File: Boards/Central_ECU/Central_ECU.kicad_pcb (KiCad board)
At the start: 4 copper layers, 100 x 100 mm, 178 parts, among them J1 Micro_SD_Card, J10 Solenoid NANOFIT, J11 DB9 Microfit, J12 RS422 JST, J13 USB_B_Micro, J14 SWD JST PH, J15 UART JST, J2 Extras JST, J3 MICROFIT, J4 Siren MICROFIT, J5 I2CB JST, J6 MICROFIT, J7 I2CA JST, J8 Ignitor JST EH, J9 DB9 MICROFIT, Q1 DMT12H060LFDF, Q2 DMT12H060LFDF, Q3 DMT12H060LFDF, Q4 DMP6023LFG, Q5 DMP6023LFG, SW2 On Switch, U1 SSD1306, U2 STM32G0B1RCTx, U3 TCAN1046, U4 LM339B, U5 LM1084-ADJ, U6 TPS16630PWPR, U7 AZ1117C-5.0, U8 AZ1117C-3.3, U9 LPS22HH, Y1 8MHz, Y2 32.768k

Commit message: More progress on layout
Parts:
- added R49: 10K, Resistor_SMD:R_0603_1608Metric, F.Cu at (147.3, 117.1)
- added R50: 10K, Resistor_SMD:R_0603_1608Metric, F.Cu at (146.6, 118.6)
- C1, C10, C2, C3, C4, C7: moved to B.Cu
- C26, C27: footprint Capacitor_SMD:C_0603_1608Metric -> Capacitor_SMD:C_1206_3216Metric
- C30, C31, C33, C34: footprint Capacitor_SMD:C_0603_1608Metric -> Capacitor_SMD:C_1206_3216Metric; moved to B.Cu
- C6, C8, C9: footprint Capacitor_SMD:C_0603_1608Metric -> Capacitor_SMD:C_0402_1005Metric
- R20, R21, R22: footprint Resistor_SMD:R_0603_1608Metric -> Resistor_SMD:R_1206_3216Metric
- TP12: value ARMSIG -> CONT2
- TP13: value EMCH1 -> CONT1
- TP15: value EMCH2 -> OXSNE
- TP17: value OXFIRE -> SNE12
- TP18: value SENSE12 -> OXFIRE
- TP19: value SENSEOX -> EMCH2
- TP20: value CONT1 -> EMCH1
- TP21: value CONT2 -> ARMSIG
- Y1: footprint Crystal:Crystal_SMD_Abracon_ABM3B-4Pin_5.0x3.2mm -> Crystal:Crystal_SMD_Abracon_ABM8G-4Pin_3.2x2.5mm
- moved R20 241.6 mm to (165.1, 55.9), turned to 90 degrees
- moved J8 237.0 mm to (165.6, 145.8)
- moved J10 227.4 mm to (187.2, 146.0), turned to -90 degrees
- moved U5 226.0 mm to (179.7, 56.4)
- moved Q3 220.5 mm to (168.1, 142.2), turned to 180 degrees
- moved R36 219.1 mm to (164.8, 142.7), turned to 180 degrees
- moved C35 219.0 mm to (164.8, 139.7)
- moved R38 218.6 mm to (164.8, 141.2)
- moved C34 217.9 mm to (167.1, 148.1)
- moved C33 217.6 mm to (167.1, 143.5)
- moved C18 217.2 mm to (187.6, 106.4), turned to 180 degrees
- moved D15 217.0 mm to (170.7, 142.7), turned to 180 degrees
- moved R37 214.3 mm to (169.2, 138.9), turned to -90 degrees
- moved R39 214.1 mm to (169.2, 135.9), turned to -90 degrees
- moved J11 213.9 mm to (192.5, 121.8), turned to 90 degrees
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- renumbered ARM to SW1
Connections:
- C29 pad 1: /EMATCH_2_CONT -> /ARM_HS
- R25 pad 1: /12V_SENSE -> /OX_FIRE
- R26 pad 2: /12V_SENSE -> /OX_FIRE
- R30 pad 1: /EMATCH_2_CONT -> /ARM_HS
- R33 pad 1: /OX_LOW_SENSE -> /EMATCH_2_FIRE
- R35 pad 2: /OX_LOW_SENSE -> /EMATCH_2_FIRE
- R37 pad 1: /EMATCH_1_CONT -> /EMATCH_1_FIRE
- R39 pad 2: /EMATCH_1_CONT -> /EMATCH_1_FIRE
- TP12 pad 1: /ARM_HS -> /EMATCH_2_CONT
- TP13 pad 1: /EMATCH_1_FIRE -> /EMATCH_1_CONT
- TP15 pad 1: /EMATCH_2_FIRE -> /OX_LOW_SENSE
- TP17 pad 1: /OX_FIRE -> /12V_SENSE
- TP18 pad 1: /12V_SENSE -> /OX_FIRE
- TP19 pad 1: /OX_LOW_SENSE -> /EMATCH_2_FIRE
- TP20 pad 1: /EMATCH_1_CONT -> /EMATCH_1_FIRE
- TP21 pad 1: /EMATCH_2_CONT -> /ARM_HS
- U2 pad 1: /OX_LOW_SENSE -> /EMATCH_2_FIRE
- U2 pad 2: /EMATCH_1_CONT -> /EMATCH_1_FIRE
- U2 pad 3: /EMATCH_2_CONT -> /ARM_HS
- U2 pad 38: /ARM_HS -> /EMATCH_2_CONT
- U2 pad 39: /EMATCH_1_FIRE -> /EMATCH_1_CONT
- U2 pad 48: /EMATCH_2_FIRE -> /OX_LOW_SENSE
- U2 pad 49: /OX_FIRE -> /12V_SENSE
- U2 pad 64: /12V_SENSE -> /OX_FIRE
- U4 pad 1: /ARM_HS -> /EMATCH_2_CONT
- U4 pad 13: /EMATCH_2_FIRE -> /OX_LOW_SENSE
- U4 pad 14: /OX_FIRE -> /12V_SENSE
- U4 pad 2: /EMATCH_1_FIRE -> /EMATCH_1_CONT
- U6 pad 13: /EMATCH_2_CONT -> /ARM_HS
- Y1 pad 2: Net-(U2-PF1) -> (no net)
- Y1 pad 3: (no net) -> Net-(U2-PF1)
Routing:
- net GND: track 0.00 -> 125.0 mm, vias 0 -> 62
- net +3V3: track 0.00 -> 62.8 mm, vias 0 -> 27
- net /CANH2: track 0.00 -> 60.8 mm
- net /Connectors/EMATCH_1+: track 0.00 -> 59.9 mm
- net /ADC_0 (4S): track 0.00 -> 58.7 mm, vias 0 -> 2
- net /Connectors/SOLENOID-: track 0.00 -> 54.6 mm
- net /EMATCH_2_FIRE: track 0.00 -> 54.0 mm, vias 0 -> 2
- net /I2C2_SCL: track 0.00 -> 52.1 mm, vias 0 -> 2
- net /EMATCH_1_FIRE: track 0.00 -> 51.3 mm, vias 0 -> 2
- net /I2C1_SDA: track 0.00 -> 51.0 mm
- net /I2C2_SDA: track 0.00 -> 49.6 mm, vias 0 -> 2
- net /I2C1_SCL: track 0.00 -> 49.1 mm
- net /CANL2: track 0.00 -> 48.5 mm
- net /I2C3_SDA: track 0.00 -> 48.4 mm
- net /ARM_HS: track 0.00 -> 48.3 mm, vias 0 -> 2
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- added copper zone on In2.Cu, net +3V3
- added copper zone on B.Cu, net GND
- added copper zone on In1.Cu, net GND

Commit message: Finished central ECU for review
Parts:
- TP1, TP10, TP11, TP12, TP13, TP14, TP15, TP16, TP17, TP18, TP2, TP21, TP24, TP25, TP26, TP29, TP3, TP30, TP4, TP5, TP6, TP7, TP8, TP9: footprint TestPoint:TestPoint_Keystone_5005-5009_Compact -> TestPoint:TestPoint_Pad_1.5x1.5mm
- TP19, TP20, TP22, TP23, TP31, TP32, TP33: footprint TestPoint:TestPoint_Keystone_5005-5009_Compact -> TestPoint:TestPoint_Pad_1.5x1.5mm; moved to B.Cu
- moved TP28 170.1 mm to (193.8, 70.1)
- moved TP8 156.1 mm to (167.9, 100.3)
- moved TP10 155.5 mm to (167.9, 108.7)
- moved TP11 152.5 mm to (168.1, 104.4)
- moved TP19 152.2 mm to (172.2, 134.9)
- moved TP15 152.1 mm to (176.0, 114.8)
- moved TP9 151.5 mm to (163.3, 104.4)
- moved TP17 146.6 mm to (172.0, 114.8)
- moved TP20 145.9 mm to (167.4, 134.9)
- moved TP21 142.7 mm to (169.2, 124.7)
- moved TP6 141.3 mm to (156.2, 122.2)
- moved TP13 140.6 mm to (165.9, 95.2)
- moved TP5 140.5 mm to (152.9, 130.3)
- moved TP12 140.5 mm to (161.8, 95.2)
- moved TP4 139.9 mm to (153.7, 118.6)
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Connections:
- TP8 pad 1: /CAN1_RX -> /CAN1_TX
- TP9 pad 1: /CAN1_TX -> /CAN1_RX
- U2 pad 32: /CAN1_AUX -> /CAN2_AUX
- U2 pad 33: /CAN2_AUX -> /CAN1_AUX
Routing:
- net +5V: track 25.0 -> 150.0 mm, vias 1 -> 3
- net +7V4: track 32.0 -> 128.4 mm, vias 0 -> 5
- net /CAN2_AUX: track 0.00 -> 49.0 mm
- net /12V_SENSE: track 0.00 -> 45.0 mm, vias 0 -> 2
- net /OX_LOW_SENSE: track 0.00 -> 43.3 mm, vias 0 -> 2
- net /EMATCH_1_CONT: track 0.00 -> 39.6 mm, vias 0 -> 2
- net /OX_FIRE: track 41.1 -> 76.7 mm, vias 0 -> 2
- net /EMATCH_2_CONT: track 0.00 -> 31.4 mm, vias 0 -> 2
- net /ADC_1 (2S): track 42.8 -> 72.7 mm
- net GND: track 125.0 -> 154.8 mm, vias 62 -> 151
- net /PGOOD_HS: track 34.3 -> 58.2 mm, vias 0 -> 2
- net /ADC_0 (4S): track 58.7 -> 81.0 mm
- net /E1: track 0.00 -> 22.1 mm
- net /IMON_HS: track 34.0 -> 55.4 mm, vias 0 -> 2
- net /E2: track 0.00 -> 20.2 mm
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- added copper zone on B.Cu, net +7V4
- added copper zone on In2.Cu, net Net-(U4D-+)
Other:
- board text added: "${CURRENT_DATE}"
- board text added: "${REVISION}"
- board text added: "2S IN"
- board text added: "4S IN"
- board text added: "B Redpath"
- board text added: "CAN1"
- board text added: "CAN2"
- board text added: "Date"
- board text added: "Drawn"
- board text added: "HYBRID CENTRAL ECU"
- board text added: "IGNITORS"
- board text added: "INTERLOCK ARM"
- board text added: "ON/OFF SWITCH"
- board text added: "Revision"
- board text added: "SOLENOID"

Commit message: Tidy up, will send to Chris
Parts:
- removed TP33: ADC4, TestPoint:TestPoint_Pad_1.5x1.5mm
- moved TP31 3.42 mm to (147.6, 115.1)
- moved TP32 2.70 mm to (150.4, 117.3)
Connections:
- U2 pad 21: /ADC_4 -> /SPI_SD_CS
- U2 pad 36: /SPI_SD_CS -> unconnected-(U2-PA8-Pad36)
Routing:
- net /SPI_SD_CS: track 44.1 -> 35.1 mm
- net /ADC_4: track 8.38 -> 0.00 mm, vias 1 -> 0
- net GND: track 154.8 -> 162.0 mm, vias 151 -> 196
- net +3V3: track 81.1 -> 86.0 mm, vias 28 -> 25
- net /OX_FIRE: track 76.7 -> 72.1 mm
- net /ADC_2: track 7.96 -> 12.3 mm
- net Net-(U4D-+): track 53.8 -> 57.5 mm, vias 4 -> 6
- net /ADC_3: track 10.6 -> 13.1 mm
- net /ARM_HS: track 51.0 -> 52.4 mm
- net /Connectors/EMATCH_1+: track 64.7 -> 65.7 mm
- net /EMATCH_2_FIRE: track 55.9 -> 56.7 mm

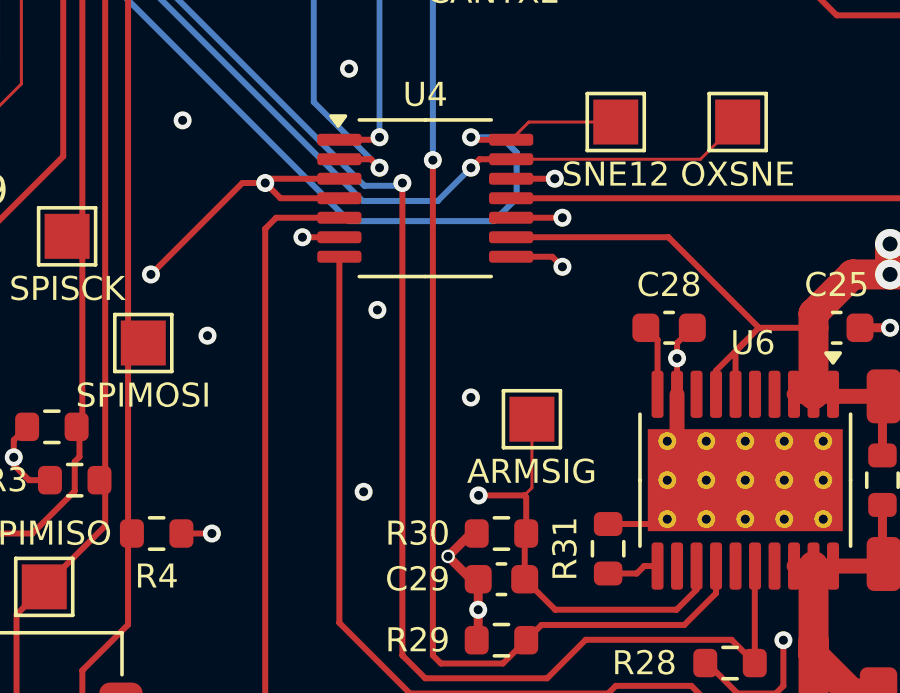
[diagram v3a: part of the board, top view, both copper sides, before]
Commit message: Fixed voltage divider and comparator bias
Re feedback from Chris still need to fix regulator power dissipation. Happy with other points being non-issues at current.
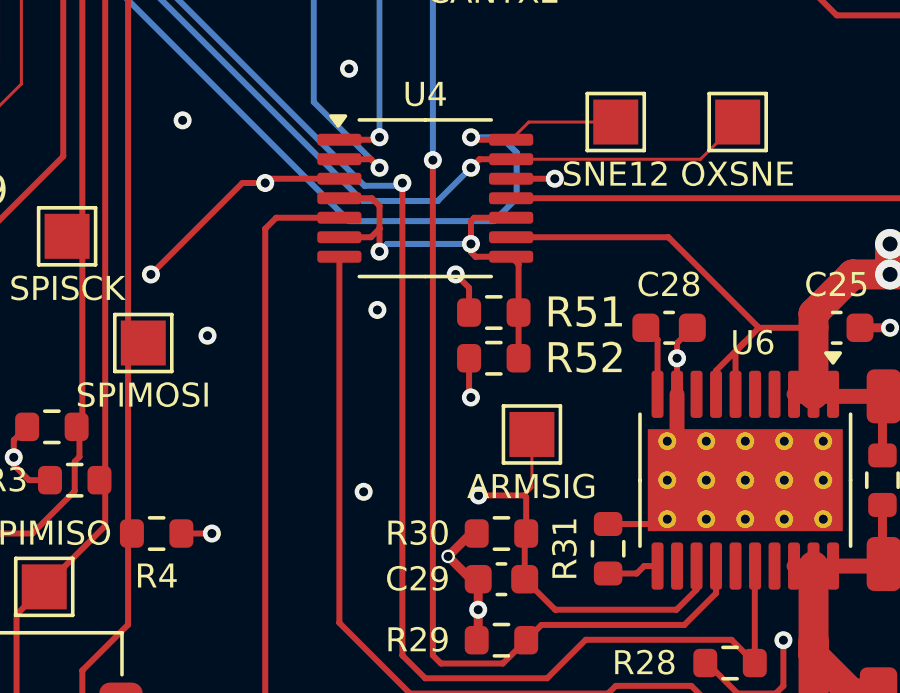
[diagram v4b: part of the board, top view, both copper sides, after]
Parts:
- added R51: 10K, Resistor_SMD:R_0603_1608Metric, F.Cu at (167.9, 121.2)
- added R52: 10K, Resistor_SMD:R_0603_1608Metric, F.Cu at (167.9, 122.7)
- R44: value 39K2 -> 10K2
- R45: value 4K32 -> 2K49
- moved TP21 0.51 mm to (169.2, 125.2)
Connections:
- U4 pad 10: +3V3 -> /Interlocked/COMP_BIAS
- U4 pad 4: +3V3 -> /Interlocked/COMP_BIAS
- U4 pad 6: +3V3 -> /Interlocked/COMP_BIAS
- U4 pad 8: +3V3 -> /Interlocked/COMP_BIAS
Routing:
- net /Interlocked/COMP_BIAS: track 0.00 -> 14.9 mm, vias 0 -> 2
- net +3V3: track 86.0 -> 79.9 mm, vias 25 -> 23
- net GND: track 162.0 -> 163.4 mm
- net /ARM_HS: track 52.4 -> 51.9 mm

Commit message: Central ECU to order
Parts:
- removed C21: 10u, Capacitor_SMD:C_0603_1608Metric
- removed C22: 50u, Capacitor_SMD:CP_Elec_6.3x9.9
- removed R24: 1K40, Resistor_SMD:R_0603_1608Metric
- removed U5: LM1084-ADJ, Package_TO_SOT_SMD:TO-263-3_TabPin2
- added C43: 100u, Capacitor_SMD:CP_Elec_8x10.5, F.Cu at (186.2, 56.9)
- added D16: 30V 34VC, Diode_SMD:D_SOD-882, F.Cu at (175.1, 62.2)
- added J16: MICROFIT, Connector_Molex:Molex_Micro-Fit_3.0_43045-0412_2x02_P3.00mm_Vertical, F.Cu at (173.8, 54.4)
- C23, C24: value 22u -> 10u; footprint Capacitor_SMD:C_0603_1608Metric -> Capacitor_SMD:C_1206_3216Metric
- C27, C30, C31, C33, C34: value 22u -> 10u
- D2: value LED -> LED_R
- D3: value LED -> LED_G
- D4: value LED -> LED_B
- R23: value 121R -> 0R; footprint Resistor_SMD:R_0603_1608Metric -> Resistor_SMD:R_1206_3216Metric
- TP29: value 12V -> SPICY+
- moved R23 80.8 mm to (180.3, 144.0), turned to -90 degrees
- moved F1 1.80 mm to (182.4, 132.1)
- moved C23 1.22 mm to (182.4, 134.6)
- moved TP29 0.36 mm to (169.7, 66.0)
- moved C24 0.27 mm to (182.4, 137.4)
- moved R22 0.25 mm to (181.1, 64.5)
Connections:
- C27 pad 1: /Connectors/EMATCH_1+ -> Net-(C27-Pad1)
- F1 pad 1: /Connectors/EMATCH_1+ -> Net-(C27-Pad1)
- R22 pad 1: Net-(U5-VO) -> Net-(D16-A2)
- R23 pad 1: Net-(U5-VO) -> Net-(C27-Pad1)
- R23 pad 2: Net-(U5-ADJ) -> /Connectors/EMATCH_1+
- R27 pad 2: /Connectors/EMATCH_1+ -> Net-(C27-Pad1)
- U6 pad 18: /Connectors/EMATCH_1+ -> Net-(C27-Pad1)
- U6 pad 19: /Connectors/EMATCH_1+ -> Net-(C27-Pad1)
- U6 pad 20: /Connectors/EMATCH_1+ -> Net-(C27-Pad1)
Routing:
- net Net-(U5-VO): track 30.5 -> 0.00 mm
- net /Connectors/EMATCH_1+: track 65.7 -> 40.8 mm
- net Net-(C27-Pad1): track 0.00 -> 21.1 mm
- net Net-(D16-A2): track 0.00 -> 19.9 mm
- net Net-(U5-ADJ): track 19.3 -> 0.00 mm
- net GND: track 163.4 -> 167.4 mm, vias 196 -> 191
- net +3V3: track 79.9 -> 78.3 mm
- net /Connectors/SOLENOID+: track 16.2 -> 17.8 mm
- net Net-(J16-Pin_1): track 6.75 -> 7.36 mm
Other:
- board text added: "2S"
- board text added: "3/6S"
- board text added: "3/6S IN"
- board text added: "BYPASS"
- board text added: "EXT REG"
- board text added: "IND"
- board text added: "REG"
- board text added: "SIREN OUT"
- board text removed: "4S IN"
